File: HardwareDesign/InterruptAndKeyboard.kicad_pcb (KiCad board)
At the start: 2 copper layers, 150 x 90 mm, 39 parts, among them J001 Conn_02x40_Odd_Even, J501 Conn_01x20, J503 Conn_01x02, U401 74HCT74, U402 74HCT11, U403 74HCT147, U404 74HCT540, U405 74HCT574, U406 74HCT32, U407 74HCT32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

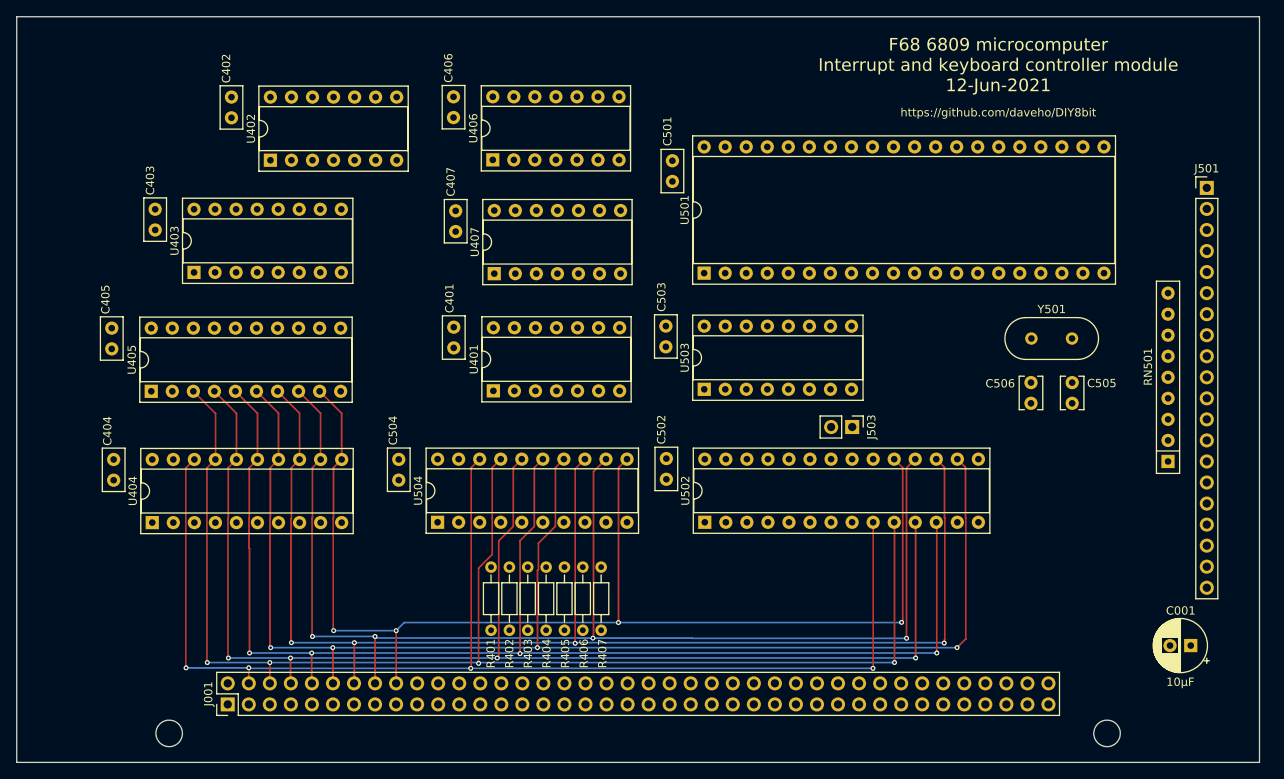
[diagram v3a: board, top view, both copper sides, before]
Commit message: routed more signals, getting there...
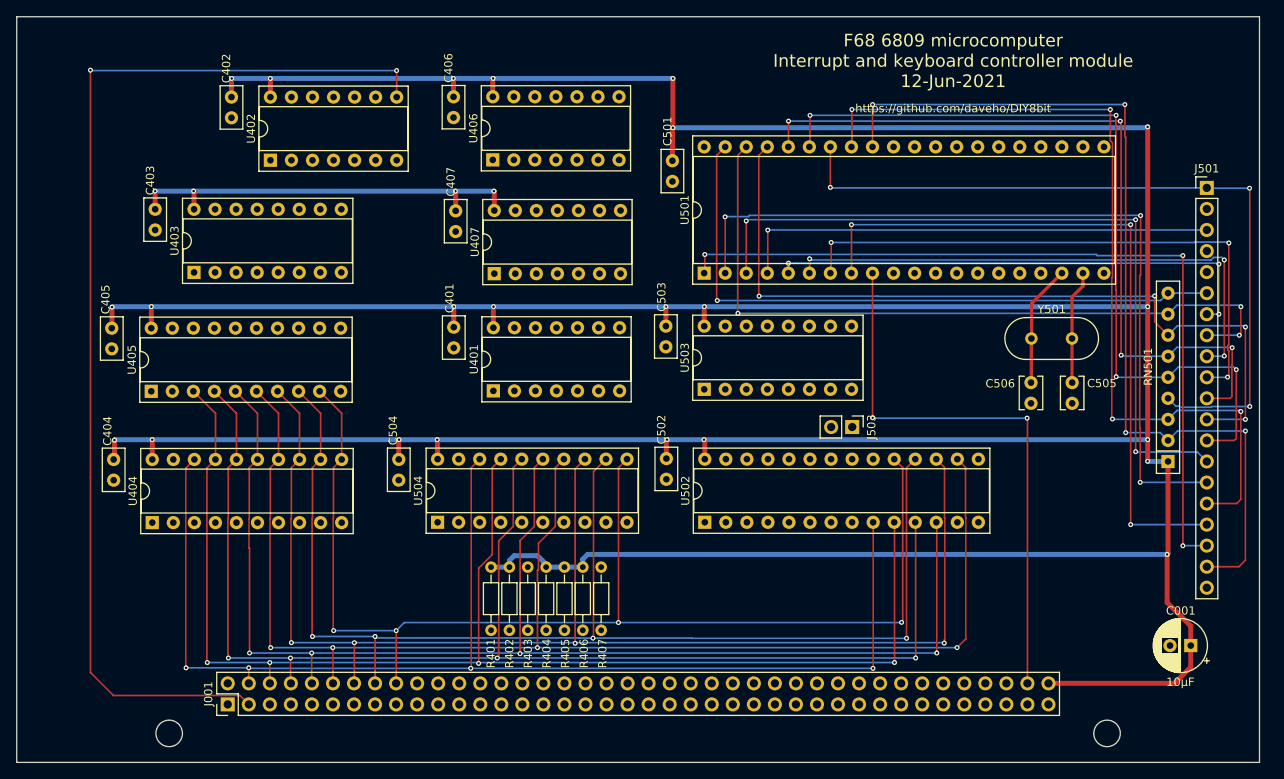
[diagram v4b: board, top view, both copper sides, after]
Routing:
- net VCC: track 0.00 -> 630.1 mm, vias 0 -> 27
- net /~IRQ: track 0.00 -> 133.6 mm, vias 0 -> 2
- net /Keyboard/ROW7: track 0.00 -> 111.1 mm, vias 0 -> 4
- net /Keyboard/ROW6: track 0.00 -> 104.2 mm, vias 0 -> 4
- net /Keyboard/ROW4: track 0.00 -> 99.5 mm, vias 0 -> 4
- net /Keyboard/COL0: track 0.00 -> 98.0 mm, vias 0 -> 3
- net /Keyboard/COL1: track 0.00 -> 97.3 mm, vias 0 -> 3
- net /Keyboard/ROW2: track 0.00 -> 97.3 mm, vias 0 -> 4
- net /Keyboard/ROW3: track 0.00 -> 94.4 mm, vias 0 -> 4
- net /Keyboard/ROW5: track 0.00 -> 92.2 mm, vias 0 -> 3
- net /Keyboard/COL2: track 0.00 -> 90.4 mm, vias 0 -> 3
- net /Keyboard/ROW1: track 0.00 -> 89.2 mm, vias 0 -> 3
- net /Keyboard/COL7: track 0.00 -> 84.9 mm, vias 0 -> 3
- net /Keyboard/ROW0: track 0.00 -> 78.5 mm, vias 0 -> 1
- net /Keyboard/COL6: track 0.00 -> 70.7 mm, vias 0 -> 3
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
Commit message: more routing...
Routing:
- net /~IODEV3: track 0.00 -> 178.9 mm, vias 0 -> 3
- net /~RMEM~: track 0.00 -> 145.8 mm, vias 0 -> 4
- net /~WMEM~: track 0.00 -> 115.3 mm, vias 0 -> 2
- net /~IRQ2~: track 0.00 -> 90.8 mm, vias 0 -> 3
- net /PC1: track 0.00 -> 87.4 mm, vias 0 -> 1
- net /~IRQ4~: track 0.00 -> 86.1 mm, vias 0 -> 5
- net /PC0: track 0.00 -> 73.5 mm, vias 0 -> 2
- net /IRQ3: track 0.00 -> 73.0 mm, vias 0 -> 4
- net /~IRQ1~: track 0.00 -> 72.9 mm, vias 0 -> 2
- net /Keyboard/~FIFO_WR: track 0.00 -> 68.6 mm, vias 0 -> 2
- net /~IRQ5~: track 0.00 -> 68.1 mm, vias 0 -> 2
- net /Keyboard/EF: track 0.00 -> 63.8 mm, vias 0 -> 1
- net /~IRQ7~: track 0.00 -> 61.8 mm
- net /IRQ6: track 0.00 -> 60.8 mm, vias 0 -> 2
- net /A0: track 0.00 -> 49.2 mm, vias 0 -> 2
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
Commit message: all non-GND traces are routed?
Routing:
- net /Keyboard/SCDAT5: track 0.00 -> 85.2 mm, vias 0 -> 2
- net /Keyboard/SCDAT1: track 0.00 -> 82.2 mm, vias 0 -> 2
- net /Keyboard/SCDAT3: track 0.00 -> 80.2 mm, vias 0 -> 1
- net /Keyboard/SCDAT0: track 0.00 -> 80.2 mm, vias 0 -> 2
- net /Keyboard/SCDAT2: track 0.00 -> 79.4 mm, vias 0 -> 3
- net /Keyboard/SCDAT4: track 0.00 -> 78.2 mm, vias 0 -> 1
- net Net-(U402-Pad13): track 0.00 -> 69.6 mm, vias 0 -> 1
- net Net-(U405-Pad16): track 0.00 -> 68.6 mm, vias 0 -> 2
- net Net-(U405-Pad17): track 0.00 -> 67.0 mm, vias 0 -> 1
- net Net-(U402-Pad3): track 0.00 -> 66.4 mm, vias 0 -> 3
- net Net-(U403-Pad9): track 0.00 -> 62.8 mm, vias 0 -> 1
- net /Keyboard/SCDAT6: track 0.00 -> 62.8 mm, vias 0 -> 1
- net Net-(U402-Pad5): track 0.00 -> 62.5 mm, vias 0 -> 3
- net /Keyboard/~RD_CTRL: track 0.00 -> 61.8 mm, vias 0 -> 2
- net Net-(U405-Pad15): track 0.00 -> 60.4 mm, vias 0 -> 2
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
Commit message: routed a couple of missed VCC nets
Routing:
- net GND: track 0.00 -> 45.0 mm, vias 0 -> 3
- net VCC: track 700.8 -> 705.4 mm, vias 32 -> 34
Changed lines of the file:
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@@
     (thickness 1.6002)
     (drawings 6)
-    (tracks 1198)
+    (tracks 1224)
     (zones 0)
     (modules 39)
@@
   )
   (setup
-    (last_trace_width 0.2)
+    (last_trace_width 0.6)
     (user_trace_width 0.15)
     (user_trace_width 0.2)
@@
   (via (at 136.5 13.3) (size 0.6) (drill 0.3) (layers Front Back) (net 1))
   (segment (start 136.4 13.4) (end 136.5 13.3) (width 0.6) (layer Back) (net 1))
-  (segment (start 79.2 13.4) (end 136.4 13.4) (width 0.6) (layer Back) (net 1))
   (segment (start 136.5 35) (end 136.5 13.3) (width 0.6) (layer Front) (net 1))
   (via (at 79.2 7.45) (size 0.6) (drill 0.3) (layers Front Back) (net 1))
@@
   (segment (start 95.8 51.05) (end 136.5 51.05) (width 0.6) (layer Back) (net 1))
   (segment (start 82.95 51.05) (end 95.8 51.05) (width 0.6) (layer Back) (net 1))
+  (via (at 82.95 13.4) (size 0.6) (drill 0.3) (layers Front Back) (net 1))
+  (segment (start 82.97 13.42) (end 82.95 13.4) (width 0.6) (layer Front) (net 1))
+  (segment (start 82.97 15.71) (end 82.97 13.42) (width 0.6) (layer Front) (net 1))
+  (segment (start 79.2 13.4) (end 82.95 13.4) (width 0.6) (layer Back) (net 1))
+  (via (at 105.8 13.4) (size 0.6) (drill 0.3) (layers Front Back) (net 1))
+  (segment (start 105.83 13.43) (end 105.8 13.4) (width 0.6) (layer Front) (net 1))
+  (segment (start 105.83 15.71) (end 105.83 13.43) (width 0.6) (layer Front) (net 1))
+  (segment (start 105.8 13.4) (end 136.4 13.4) (width 0.6) (layer Back) (net 1))
+  (segment (start 82.95 13.4) (end 105.8 13.4) (width 0.6) (layer Back) (net 1))
+  (via (at 60.05 39.95) (size 0.6) (drill 0.3) (layers Front Back) (net 2))
+  (segment (start 60.03 39.97) (end 60.05 39.95) (width 0.6) (layer Back) (net 2))
+  (segment (start 52.75 39.97) (end 60.03 39.97) (width 0.6) (layer Back) (net 2))
+  (segment (start 60.05 45.14) (end 60.07 45.16) (width 0.6) (layer Front) (net 2))
+  (segment (start 60.05 39.95) (end 60.05 45.14) (width 0.6) (layer Front) (net 2))
+  (segment (start 60.05 39.95) (end 62.05 39.95) (width 0.6) (layer Back) (net 2))
+  (segment (start 62.61 39.39) (end 62.61 37.54) (width 0.6) (layer Back) (net 2))
+  (segment (start 62.05 39.95) (end 62.61 39.39) (width 0.6) (layer Back) (net 2))
+  (via (at 45.85 25.95) (size 0.6) (drill 0.3) (layers Front Back) (net 2))
+  (segment (start 45.86 25.94) (end 45.85 25.95) (width 0.6) (layer Front) (net 2))
+  (segment (start 45.86 17.32) (end 45.86 25.94) (width 0.6) (layer Front) (net 2))
+  (segment (start 52.96 25.95) (end 52.98 25.93) (width 0.6) (layer Back) (net 2))
+  (segment (start 45.85 25.95) (end 52.96 25.95) (width 0.6) (layer Back) (net 2))
+  (via (at 45.85 12.15) (size 0.6) (drill 0.3) (layers Front Back) (net 2))
+  (segment (start 45.87 12.17) (end 45.85 12.15) (width 0.6) (layer Back) (net 2))
+  (segment (start 52.72 12.17) (end 45.87 12.17) (width 0.6) (layer Back) (net 2))
+  (segment (start 45.85 17.31) (end 45.86 17.32) (width 0.6) (layer Front) (net 2))
+  (segment (start 45.85 12.15) (end 45.85 17.31) (width 0.6) (layer Front) (net 2))
   (segment (start 44.712999 10.847001) (end 44.712999 84.237001) (width 0.2) (layer Front) (net 5))
   (segment (start 45.86 9.7) (end 44.712999 10.847001) (width 0.2) (layer Front) (net 5))

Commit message: all connections routed?
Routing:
- net GND: track 45.0 -> 82.5 mm, vias 3 -> 4
- added copper zone on B.Cu, net GND
- added copper zone on F.Cu, net GND
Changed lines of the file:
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@@
     (thickness 1.6002)
     (drawings 6)
-    (tracks 1224)
+    (tracks 1237)
     (zones 0)
     (modules 39)
@@
   (segment (start 45.85 17.31) (end 45.86 17.32) (width 0.6) (layer Front) (net 2))
   (segment (start 45.85 12.15) (end 45.85 17.31) (width 0.6) (layer Front) (net 2))
+  (via (at 85.55 55.85) (size 0.6) (drill 0.3) (layers Front Back) (net 2))
+  (segment (start 85.59 55.89) (end 85.55 55.85) (width 0.6) (layer Front) (net 2))
+  (segment (start 85.59 61.02) (end 85.59 55.89) (width 0.6) (layer Front) (net 2))
+  (segment (start 78.43 55.85) (end 78.41 55.83) (width 0.6) (layer Back) (net 2))
+  (segment (start 85.55 55.85) (end 78.43 55.85) (width 0.6) (layer Back) (net 2))
+  (segment (start 58.42 61.02) (end 60.96 61.02) (width 0.6) (layer Back) (net 2))
+  (segment (start 60.96 61.02) (end 63.5 61.02) (width 0.6) (layer Back) (net 2))
+  (segment (start 63.5 61.02) (end 66.04 61.02) (width 0.6) (layer Back) (net 2))
+  (segment (start 66.04 61.02) (end 68.58 61.02) (width 0.6) (layer Back) (net 2))
+  (segment (start 68.58 61.02) (end 71.12 61.02) (width 0.6) (layer Back) (net 2))
+  (segment (start 71.12 61.02) (end 73.66 61.02) (width 0.6) (layer Back) (net 2))
+  (segment (start 73.66 61.02) (end 78.38 61.02) (width 0.6) (layer Back) (net 2))
+  (segment (start 78.41 60.99) (end 78.41 55.83) (width 0.6) (layer Back) (net 2))
+  (segment (start 78.38 61.02) (end 78.41 60.99) (width 0.6) (layer Back) (net 2))
   (segment (start 44.712999 10.847001) (end 44.712999 84.237001) (width 0.2) (layer Front) (net 5))
   (segment (start 45.86 9.7) (end 44.712999 10.847001) (width 0.2) (layer Front) (net 5))
@@
   (segment (start 61.1 22.05) (end 60.18 22.97) (width 0.2) (layer Back) (net 55))
   (segment (start 61.1 22.05) (end 52.840038 22.05) (width 0.2) (layer Back) (net 55))
-  (segment (start 19.75 36.85) (end 19.807001 36.907001) (width 0.2) (layer Front) (net 55))
   (via (at 18.9 50.3) (size 0.6) (drill 0.3) (layers Front Back) (net 55))
   (segment (start 18.9 53.44) (end 18.9 50.3) (width 0.2) (layer Front) (net 55))
@@
   (segment (start 49.772999 59.992999) (end 50.8 61.02) (width 0.2) (layer Front) (net 157))
   (segment (start 50.4 41.4) (end 49.772999 42.027001) (width 0.2) (layer Front) (net 157))
+  (zone (net 2) (net_name GND) (layer Back) (hatch edge 0.508)
+    (connect_pads (clearance 0.508))
+    (min_thickness 0.254)
+    (fill yes (arc_segments 32) (thermal_gap 0.508) (thermal_bridge_width 0.508))
+    (polygon
+      (pts
+        (xy 150 90) (xy 0 90) (xy 0 0) (xy 150 0)
+      )
+    )
+  )
+  (zone (net 2) (net_name GND) (layer Front) (hatch edge 0.508)
+    (connect_pads no (clearance 0.508))
+    (min_thickness 0.254)
+    (fill yes (arc_segments 32) (thermal_gap 0.508) (thermal_bridge_width 0.508))
+    (polygon
+      (pts
+        (xy 150 90) (xy 0 90) (xy 0 0) (xy 150 0)
+      )
+    )
+  )
 )
